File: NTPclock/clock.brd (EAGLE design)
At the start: 160 x 100 mm, 20 parts, among them IC1 MAX7219CNG

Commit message: Initial board layout
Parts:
- added R3: 10KΩ, SparkFun-Resistors:1206
- C6: device SparkFun-Capacitors:CPOL-RADIAL-1000UF-25V -> SparkFun-Capacitors:CPOL-RADIAL-100UF-25V
- moved J1 55.7 mm to (-3.00, 41.0), turned to 180 degrees
- moved BAR_GRAPH 50.4 mm to (88.0, 62.2)
- moved DIG_0 49.2 mm to (16.0, 62.0)
- moved DIG_1 49.2 mm to (34.0, 62.0)
- moved DIG_2 49.2 mm to (55.0, 62.0)
- moved DIG_3 49.2 mm to (73.0, 62.0)
- moved C5 48.8 mm to (-4.00, 45.0), turned to 0 degrees
- moved C2 47.8 mm to (41.8, 8.00), turned to 180 degrees
- moved R1 47.4 mm to (75.0, 15.0), turned to 90 degrees
- moved DOUT 46.4 mm to (58.0, 16.0)
- moved C7 46.3 mm to (35.5, 4.75)
- moved R2 43.2 mm to (78.0, 15.0), turned to 90 degrees
- moved IC1 38.6 mm to (70.8, 29.6)
- moved U$1 36.4 mm to (25.0, 22.6), turned to 90 degrees
- moved C4 36.1 mm to (30.0, 7.00), turned to 90 degrees
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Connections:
- removed net +3.3V: C5.1, J1.2
- removed net +5V: C1.1, C2.1, C3.1, C4.1, C6.+, C7.1, C8.1, IC1.19, POWER.1, R2.2, U$1.VIN
- new net 3.3V: C5.1, J1.2, R3.1, U$1.3V3@0, U$1.3V3@1, U$1.3V3@2
- new net VCC: C1.1, C2.1, C3.1, C4.1, C6.1, C7.1, C8.1, IC1.19, POWER.1, R2.2, U$1.VIN
- net GND: now also C6.2; no longer C6.-
- net SQL: now also R3.2
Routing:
- net D: track 0.00 -> 117.9 mm, vias 0 -> 4
- net A: track 0.00 -> 101.4 mm, vias 0 -> 4
- net C: track 0.00 -> 99.8 mm, vias 0 -> 3
- net B: track 0.00 -> 92.8 mm
- net DP: track 0.00 -> 91.7 mm, vias 0 -> 2
- net E: track 0.00 -> 90.0 mm, vias 0 -> 3
- net G: track 0.00 -> 90.0 mm, vias 0 -> 3
- net F: track 0.00 -> 81.8 mm, vias 0 -> 3
- net DIGIT3: track 0.00 -> 20.3 mm
- net DIGIT2: track 0.00 -> 20.3 mm
- net DIGIT1: track 0.00 -> 20.3 mm
- net DIGIT0: track 0.00 -> 20.3 mm
- net DIGIT4: track 0.00 -> 10.2 mm
- net DIGIT5: track 0.00 -> 10.2 mm
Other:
- board size 160 x 100 mm -> 100 x 100 mm

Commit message: Board update
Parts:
- C6: value (none) -> 470μF
- moved POWER 92.0 mm to (96.0, 5.00)
- moved C1 81.0 mm to (91.0, 5.00)
- moved C6 69.0 mm to (85.0, 5.00)
- moved DOUT 43.9 mm to (25.0, 45.0)
- moved C4 30.0 mm to (60.0, 6.00)
- moved IC1 29.2 mm to (43.8, 40.6)
- moved C3 22.2 mm to (80.0, 30.0), turned to 0 degrees
- moved C8 20.4 mm to (80.0, 35.0), turned to 180 degrees
- moved R1 20.2 mm to (68.0, 34.0)
- moved R2 19.9 mm to (72.0, 34.0)
- moved C7 19.0 mm to (54.5, 5.75)
- moved U$1 8.06 mm to (26.0, 14.6)
- moved C2 2.24 mm to (42.8, 6.00), flipped to the bottom, turned to 0 degrees

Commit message: Update Boardfile.  (Also break it)
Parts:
- U$1: value ESP12E_DEVKIT -> NODEMCU V3
- moved C3 28.6 mm to (53.0, 39.5), flipped to the bottom
- moved R2 22.5 mm to (54.0, 47.5), turned to 180 degrees
- moved R1 16.0 mm to (59.5, 47.5), turned to 0 degrees
- moved IC1 13.0 mm to (56.8, 39.6)
- moved DOUT 7.07 mm to (18.0, 44.0)
- moved C8 6.21 mm to (76.0, 39.8), turned to 90 degrees
- moved C4 1.00 mm to (60.0, 5.00)
- moved C7 0.75 mm to (54.5, 5.00)
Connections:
- net CLK: now also U$1.D7; no longer U$1.D6
- net DIGIT0: no longer DIG_3.3, DIG_3.8
- net DIGIT1: now also DIG_1.3, DIG_1.8; no longer DIG_2.3, DIG_2.8
- net DIGIT2: no longer DIG_1.3, DIG_1.8
- net DIGIT4: now also DIG_2.3, DIG_2.8
- net DIGIT5: now also DIG_3.3, DIG_3.8
- net LOAD: now also U$1.D6; no longer U$1.D7
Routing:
- net GND: track 0.00 -> 136.9 mm
- net VCC: track 0.00 -> 92.3 mm
- net CLK: track 0.00 -> 57.3 mm
- net DIGIT5: track 10.2 -> 67.1 mm
- net DIGIT3: track 20.3 -> 72.4 mm
- net LOAD: track 0.00 -> 49.0 mm
- net 3.3V: track 0.00 -> 45.0 mm
- net DIGIT4: track 10.2 -> 54.3 mm
- net DIGIT1: track 20.3 -> 64.2 mm
- net A: track 101.4 -> 128.8 mm
- net B: track 92.8 -> 119.7 mm, vias 0 -> 1
- net DATA: track 0.00 -> 22.7 mm
- net F: track 81.8 -> 104.4 mm, vias 3 -> 4
- net G: track 90.0 -> 111.2 mm, vias 3 -> 4
- net DIGIT2: track 20.3 -> 0.00 mm
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
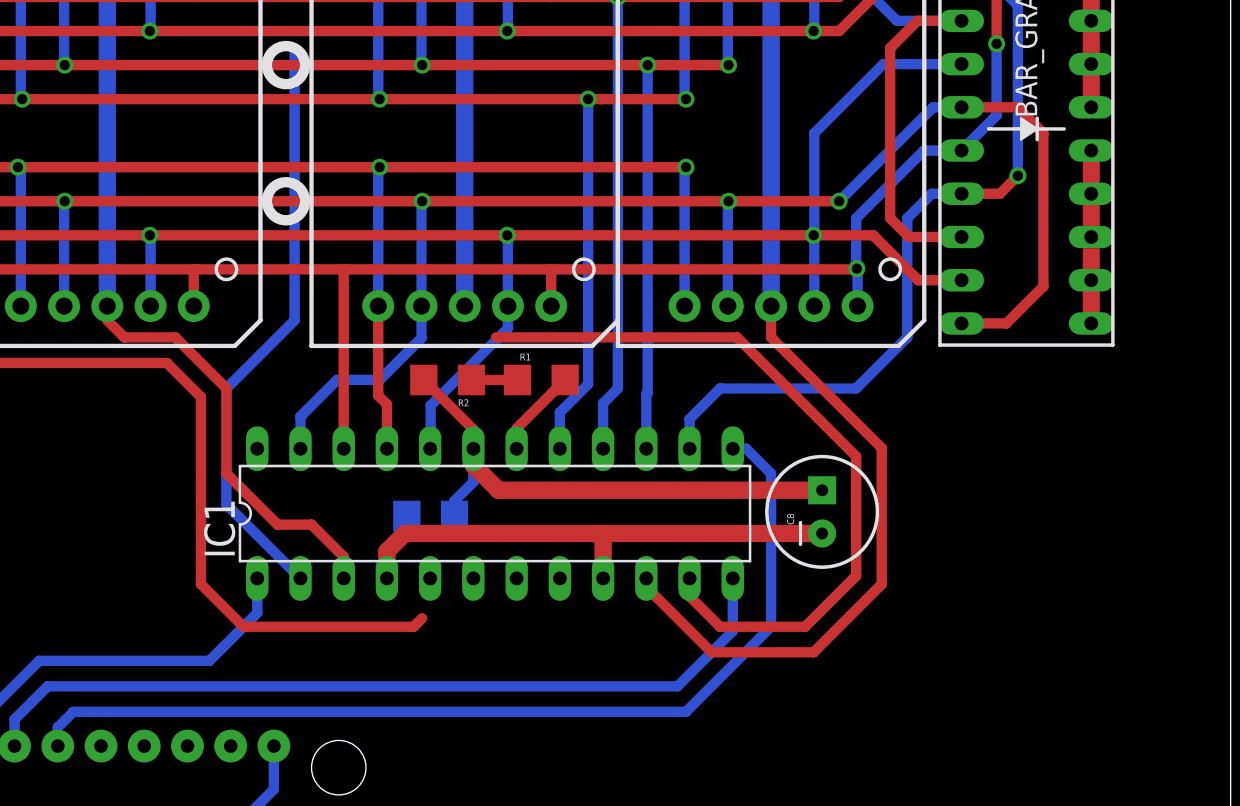
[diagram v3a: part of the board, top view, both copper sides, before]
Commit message: rearange digits
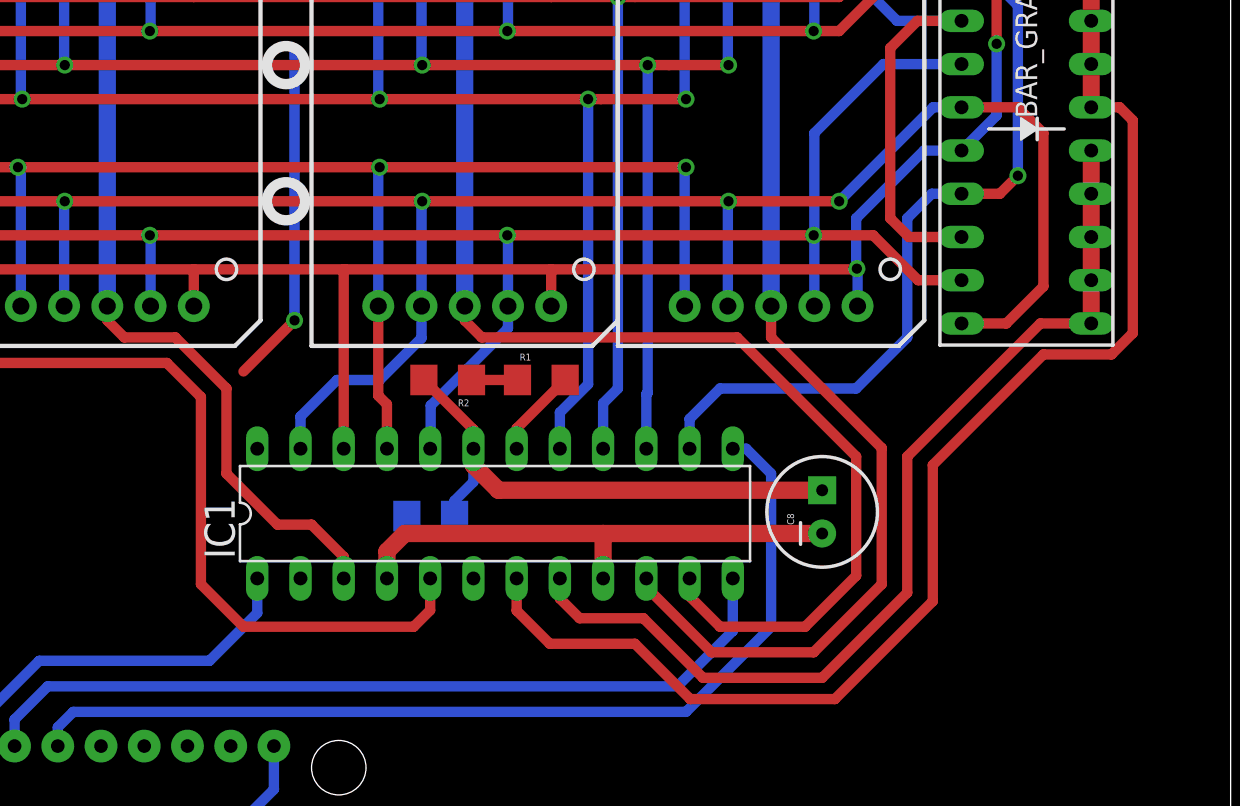
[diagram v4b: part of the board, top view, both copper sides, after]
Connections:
- net DIGIT1: now also DIG_2.3, DIG_2.8; no longer DIG_1.3, DIG_1.8
- net DIGIT3: now also BAR_GRAPH.16, BAR_GRAPH.17, BAR_GRAPH.18, BAR_GRAPH.19, BAR_GRAPH.20; no longer DIG_0.3, DIG_0.8
- net DIGIT4: now also DIG_1.3, DIG_1.8; no longer BAR_GRAPH.16, BAR_GRAPH.17, BAR_GRAPH.18, BAR_GRAPH.19, BAR_GRAPH.20, DIG_2.3, DIG_2.8
- net DIGIT5: no longer BAR_GRAPH.11, BAR_GRAPH.12, BAR_GRAPH.13, BAR_GRAPH.14, BAR_GRAPH.15
- net DIGIT6: now also DIG_0.3, DIG_0.8
- net DIGIT7: now also BAR_GRAPH.11, BAR_GRAPH.12, BAR_GRAPH.13, BAR_GRAPH.14, BAR_GRAPH.15
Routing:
- net DIGIT6: track 0.00 -> 74.9 mm
- net DIGIT7: track 0.00 -> 57.8 mm
- net DIGIT0: track 34.6 -> 20.2 mm, vias 0 -> 1
- net DIGIT5: track 67.1 -> 56.9 mm
- net DIGIT4: track 54.3 -> 45.0 mm
- net DIGIT3: track 72.4 -> 79.3 mm
- net DIGIT1: track 64.2 -> 67.3 mm
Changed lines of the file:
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@@
 <signal name="DIGIT0">
 <contactref element="IC1" pad="2"/>
-<wire x1="45.35" y1="35.84" x2="41" y2="40.19" width="0.6096" layer="16"/>
-<wire x1="41" y1="40.19" x2="41" y2="47" width="0.6096" layer="16"/>
-<wire x1="41" y1="47" x2="45" y2="51" width="0.6096" layer="16"/>
+<wire x1="41" y1="40.19" x2="41" y2="47" width="0" layer="19" extent="1-16"/>
 <wire x1="45" y1="51" x2="45" y2="67" width="0.6096" layer="16"/>
+<wire x1="41" y1="40.19" x2="45.35" y2="35.84" width="0" layer="19" extent="16-16"/>
+<via x="45" y="51" extent="1-16" drill="0.6" diameter="0.8"/>
+<wire x1="45" y1="51" x2="42" y2="48" width="0.6096" layer="1"/>
+<wire x1="42" y1="48" x2="45.35" y2="35.84" width="0" layer="19" extent="1-16"/>
 </signal>
 <signal name="DIGIT1">
 <contactref element="IC1" pad="11"/>
-<wire x1="56.84" y1="50" x2="71" y2="50" width="0.6096" layer="1"/>
+<wire x1="56" y1="50" x2="71" y2="50" width="0.6096" layer="1"/>
 <wire x1="71" y1="50" x2="78" y2="43" width="0.6096" layer="1"/>
 <wire x1="78" y1="43" x2="78" y2="36" width="0.6096" layer="1"/>
@@
 <wire x1="70" y1="33" x2="68.21" y2="34.79" width="0.6096" layer="1"/>
 <wire x1="68.21" y1="34.79" x2="68.21" y2="35.84" width="0.6096" layer="1"/>
-<contactref element="DIG_1" pad="3"/>
-<contactref element="DIG_1" pad="8"/>
-<wire x1="34" y1="72.16" x2="34" y2="51.84" width="1.016" layer="16"/>
-<wire x1="34" y1="51.84" x2="56.84" y2="50" width="0" layer="19" extent="1-1"/>
+<contactref element="DIG_2" pad="3"/>
+<contactref element="DIG_2" pad="8"/>
+<wire x1="55" y1="72.16" x2="55" y2="51.84" width="1.016" layer="16"/>
+<wire x1="56" y1="50" x2="55" y2="51" width="0.6096" layer="1"/>
+<wire x1="55" y1="51" x2="55" y2="51.84" width="0.6096" layer="1"/>
 </signal>
 <signal name="DIGIT2">
@@
 </signal>
 <signal name="DIGIT3">
-<contactref element="DIG_0" pad="3"/>
-<contactref element="DIG_0" pad="8"/>
 <contactref element="IC1" pad="7"/>
-<wire x1="16" y1="72.16" x2="16" y2="51.84" width="1.016" layer="16"/>
-<wire x1="16" y1="51.84" x2="16" y2="50" width="0.6096" layer="1"/>
-<wire x1="16" y1="50" x2="17.5" y2="48.5" width="0.6096" layer="1"/>
-<wire x1="37.5" y1="48.5" x2="39.5" y2="46.5" width="0.6096" layer="1"/>
-<wire x1="39.5" y1="46.5" x2="39.5" y2="35.5" width="0.6096" layer="1"/>
-<wire x1="39.5" y1="35.5" x2="42" y2="33" width="0.6096" layer="1"/>
-<wire x1="17.5" y1="48.5" x2="37.5" y2="48.5" width="0.6096" layer="1"/>
-<wire x1="42" y1="33" x2="52" y2="33" width="0.6096" layer="1"/>
-<wire x1="52" y1="33" x2="52.5" y2="33.5" width="0.6096" layer="1"/>
-<wire x1="52.5" y1="33.5" x2="58.05" y2="35.84" width="0" layer="19" extent="1-1"/>
+<contactref element="BAR_GRAPH" pad="16"/>
+<contactref element="BAR_GRAPH" pad="17"/>
+<contactref element="BAR_GRAPH" pad="20"/>
+<contactref element="BAR_GRAPH" pad="19"/>
+<contactref element="BAR_GRAPH" pad="18"/>
+<wire x1="91.81" y1="73.68" x2="91.81" y2="71.14" width="1" layer="1"/>
+<wire x1="91.81" y1="71.14" x2="91.81" y2="68.6" width="1" layer="1"/>
+<wire x1="91.81" y1="68.6" x2="91.81" y2="66.06" width="1" layer="1"/>
+<wire x1="91.81" y1="66.06" x2="91.81" y2="63.52" width="1" layer="1"/>
+<wire x1="91.81" y1="63.52" x2="93.48" y2="63.52" width="0.6096" layer="1"/>
+<wire x1="93.48" y1="63.52" x2="94.25" y2="62.75" width="0.6096" layer="1"/>
+<wire x1="94.25" y1="62.75" x2="94.25" y2="50.25" width="0.6096" layer="1"/>
+<wire x1="94.25" y1="50.25" x2="93" y2="49" width="0.6096" layer="1"/>
+<wire x1="93" y1="49" x2="89" y2="49" width="0.6096" layer="1"/>
+<wire x1="89" y1="49" x2="82.5" y2="42.5" width="0.6096" layer="1"/>
+<wire x1="82.5" y1="42.5" x2="82.5" y2="34.5" width="0.6096" layer="1"/>
+<wire x1="82.5" y1="34.5" x2="76.75" y2="28.75" width="0.6096" layer="1"/>
+<wire x1="76.75" y1="28.75" x2="68.25" y2="28.75" width="0.6096" layer="1"/>
+<wire x1="68.25" y1="28.75" x2="65" y2="32" width="0.6096" layer="1"/>
+<wire x1="65" y1="32" x2="60" y2="32" width="0.6096" layer="1"/>
+<wire x1="60" y1="32" x2="58.05" y2="33.95" width="0.6096" layer="1"/>
+<wire x1="58.05" y1="33.95" x2="58.05" y2="35.84" width="0.6096" layer="1"/>
 </signal>
 <signal name="A">
@@
 <signal name="DIGIT7">
 <contactref element="IC1" pad="8"/>
-</signal>
-<signal name="DIGIT6">
-<contactref element="IC1" pad="5"/>
-</signal>
-<signal name="DIGIT5">
-<contactref element="IC1" pad="10"/>
 <contactref element="BAR_GRAPH" pad="12"/>
 <contactref element="BAR_GRAPH" pad="15"/>
@@
 <wire x1="91.81" y1="55.9" x2="91.81" y2="58.44" width="1" layer="1"/>
 <wire x1="91.81" y1="58.44" x2="91.81" y2="60.98" width="1" layer="1"/>
+<wire x1="91.81" y1="50.82" x2="88.82" y2="50.82" width="0.6096" layer="1"/>
+<wire x1="88.82" y1="50.82" x2="81" y2="43" width="0.6096" layer="1"/>
+<wire x1="81" y1="43" x2="81" y2="35" width="0.6096" layer="1"/>
+<wire x1="81" y1="35" x2="76" y2="30" width="0.6096" layer="1"/>
+<wire x1="76" y1="30" x2="69" y2="30" width="0.6096" layer="1"/>
+<wire x1="69" y1="30" x2="65.5" y2="33.5" width="0.6096" layer="1"/>
+<wire x1="65.5" y1="33.5" x2="61.75" y2="33.5" width="0.6096" layer="1"/>
+<wire x1="61.75" y1="33.5" x2="60.59" y2="34.66" width="0.6096" layer="1"/>
+<wire x1="60.59" y1="34.66" x2="60.59" y2="35.84" width="0.6096" layer="1"/>
+</signal>
+<signal name="DIGIT6">
+<contactref element="IC1" pad="5"/>
+<contactref element="DIG_0" pad="3"/>
+<contactref element="DIG_0" pad="8"/>
+<wire x1="16" y1="72.16" x2="16" y2="51.84" width="1.016" layer="16"/>
+<wire x1="16" y1="51.84" x2="16" y2="50" width="0.6096" layer="1"/>
+<wire x1="16" y1="50" x2="17.5" y2="48.5" width="0.6096" layer="1"/>
+<wire x1="37.5" y1="48.5" x2="39.5" y2="46.5" width="0.6096" layer="1"/>
+<wire x1="39.5" y1="46.5" x2="39.5" y2="35.5" width="0.6096" layer="1"/>
+<wire x1="39.5" y1="35.5" x2="42" y2="33" width="0.6096" layer="1"/>
+<wire x1="17.5" y1="48.5" x2="37.5" y2="48.5" width="0.6096" layer="1"/>
+<wire x1="42" y1="33" x2="52" y2="33" width="0.6096" layer="1"/>
+<wire x1="52" y1="33" x2="52.97" y2="33.97" width="0.6096" layer="1"/>
+<wire x1="52.97" y1="33.97" x2="52.97" y2="35.84" width="0.6096" layer="1"/>
+</signal>
+<signal name="DIGIT5">
+<contactref element="IC1" pad="10"/>
 <contactref element="DIG_3" pad="3"/>
 <contactref element="DIG_3" pad="8"/>
@@
 <wire x1="65.67" y1="35.33" x2="69.5" y2="31.5" width="0.6096" layer="1"/>
 <wire x1="69.5" y1="31.5" x2="75.5" y2="31.5" width="0.6096" layer="1"/>
-<wire x1="79.5" y1="43.5" x2="91.81" y2="50.82" width="0" layer="19" extent="1-1"/>
 </signal>
 <signal name="DIGIT4">
 <contactref element="IC1" pad="3"/>
-<contactref element="BAR_GRAPH" pad="16"/>
-<contactref element="BAR_GRAPH" pad="17"/>
-<contactref element="BAR_GRAPH" pad="20"/>
-<contactref element="BAR_GRAPH" pad="19"/>
-<contactref element="BAR_GRAPH" pad="18"/>
-<wire x1="91.81" y1="73.68" x2="91.81" y2="71.14" width="1" layer="1"/>
-<wire x1="91.81" y1="71.14" x2="91.81" y2="68.6" width="1" layer="1"/>
-<wire x1="91.81" y1="68.6" x2="91.81" y2="66.06" width="1" layer="1"/>
-<wire x1="91.81" y1="66.06" x2="91.81" y2="63.52" width="1" layer="1"/>
-<contactref element="DIG_2" pad="3"/>
-<contactref element="DIG_2" pad="8"/>
-<wire x1="55" y1="72.16" x2="55" y2="51.84" width="1.016" layer="16"/>
 <wire x1="44" y1="39" x2="41" y2="42" width="0.6096" layer="1"/>
 <wire x1="34" y1="51" x2="35" y2="50" width="0.6096" layer="1"/>
@@
 <wire x1="47.89" y1="35.84" x2="47.89" y2="37.11" width="0.6096" layer="1"/>
 <wire x1="47.89" y1="37.11" x2="46" y2="39" width="0.6096" layer="1"/>
-<wire x1="55" y1="72.16" x2="91.81" y2="71.14" width="0" layer="19" extent="1-1"/>
-<wire x1="41" y1="47" x2="55" y2="51.84" width="0" layer="19" extent="1-1"/>
+<contactref element="DIG_1" pad="3"/>
+<contactref element="DIG_1" pad="8"/>
+<wire x1="34" y1="72.16" x2="34" y2="51.84" width="1.016" layer="16"/>
+<wire x1="34" y1="51" x2="34" y2="51.84" width="0.6096" layer="1"/>
 </signal>
 <signal name="DATA">
@@
 <wire x1="20.93" y1="25.99" x2="33.63" y2="13.29" width="0.6096" layer="16"/>
 <wire x1="33.63" y1="13.29" x2="33.63" y2="3.13" width="0.6096" layer="16"/>
-<wire x1="-5.54" y1="41" x2="20.93" y2="25.99" width="0" layer="19" extent="1-1"/>
-<wire x1="-5.4" y1="45" x2="-5.54" y2="41" width="0" layer="19" extent="1-1"/>
-<wire x1="-9.6" y1="45" x2="-5.4" y2="45" width="0" layer="19" extent="1-1"/>
 <wire x1="33.63" y1="13.29" x2="43.79" y2="23.45" width="0.6096" layer="16"/>
 <wire x1="43.79" y1="23.45" x2="43.79" y2="25.99" width="0.6096" layer="16"/>
+<wire x1="-5.54" y1="41" x2="-5.4" y2="45" width="0" layer="19" extent="1-1"/>
+<wire x1="-9.6" y1="45" x2="-5.4" y2="45" width="0" layer="19" extent="1-1"/>
+<wire x1="20.93" y1="25.99" x2="-5.54" y2="41" width="0" layer="19" extent="1-1"/>
 </signal>
 </signals>
